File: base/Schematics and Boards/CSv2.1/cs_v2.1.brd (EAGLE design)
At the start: 38.1 x 47 mm, 77 parts, among them J101 J-JTAG-CORTEX-NEEDLE6-LEGS, J301 HIROSE-DF40_50-PIN_CONNECTORS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, J302 HIROSE-DF40_50-PIN_CONNECTORS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, Q1 DMG3415UFY4Q-7F, U1 NCP708MU330TAG, U101 ATSAMD51, U2 W25N01GVZEIG, U201 COULOMB-MAX17262, U202 MAX77827BEWC+T, U203 SENSOR-SI7006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

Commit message: CS-main-v2.1 Routed to completion
Still need to add ground plugs.
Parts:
- moved C111 0.41 mm to (22.8, 19.5)
- moved C105 0.41 mm to (21.8, 19.5)
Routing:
- net GND: track 17.2 -> 207.0 mm, vias 4 -> 13
- net NRESET: track 0.00 -> 54.4 mm, vias 0 -> 2
- net DBG_SWCLK: track 0.00 -> 41.9 mm, vias 0 -> 3
- net DBG_SWDIO: track 0.00 -> 40.5 mm, vias 0 -> 4
- net DBG_TRACE_D0/GPIO13: track 0.00 -> 37.1 mm, vias 0 -> 1
- net DBG_DTR1_V_SENSE: track 0.00 -> 33.8 mm, vias 0 -> 2
- net DBG_DTR0_V_SENSE: track 0.00 -> 31.4 mm, vias 0 -> 2
- net DTR_MSTR_I2C_SCL_SERCOM7_P1: track 81.5 -> 110.9 mm, vias 2 -> 6
- net DBG_PROC_V_SENSE: track 1.91 -> 30.4 mm, vias 0 -> 1
- net DBG_GPIO4/SERCOM6_P0: track 0.00 -> 27.5 mm, vias 0 -> 2
- net DBG_GPIO6/SERCOM6_P2: track 0.00 -> 25.9 mm, vias 0 -> 2
- net DBG_TRACE_D2/GPIO15: track 0.00 -> 25.9 mm, vias 0 -> 3
- net STOR_QSPI_D3: track 0.00 -> 25.8 mm, vias 0 -> 2
- net DBG_SERIAL_RX_SERCOM4: track 0.00 -> 25.0 mm, vias 0 -> 3
- net DTR_MSTR_I2C_SDA_SERCOM7_P0: track 80.0 -> 104.8 mm, vias 2 -> 5
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
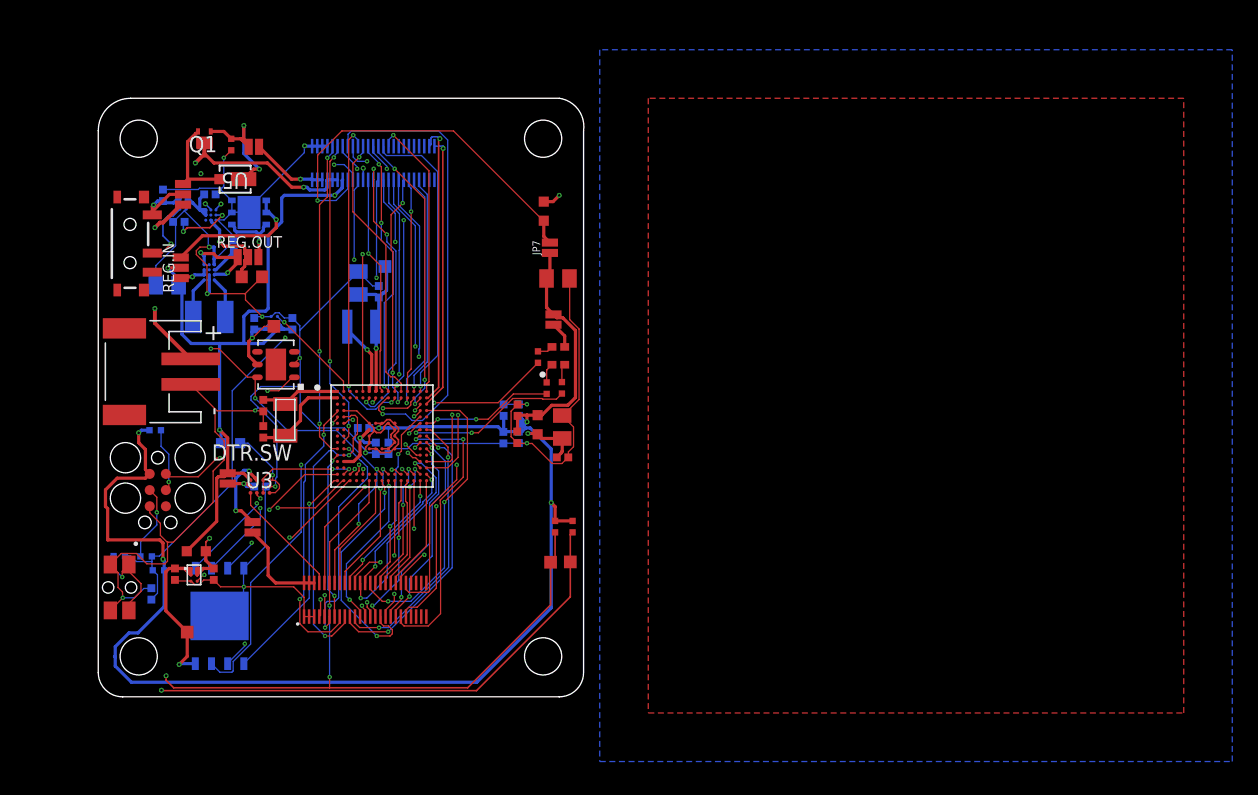
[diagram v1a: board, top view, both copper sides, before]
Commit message: CS_main-v2.1: Finish routing, add ground plugs, and fix DRC errors
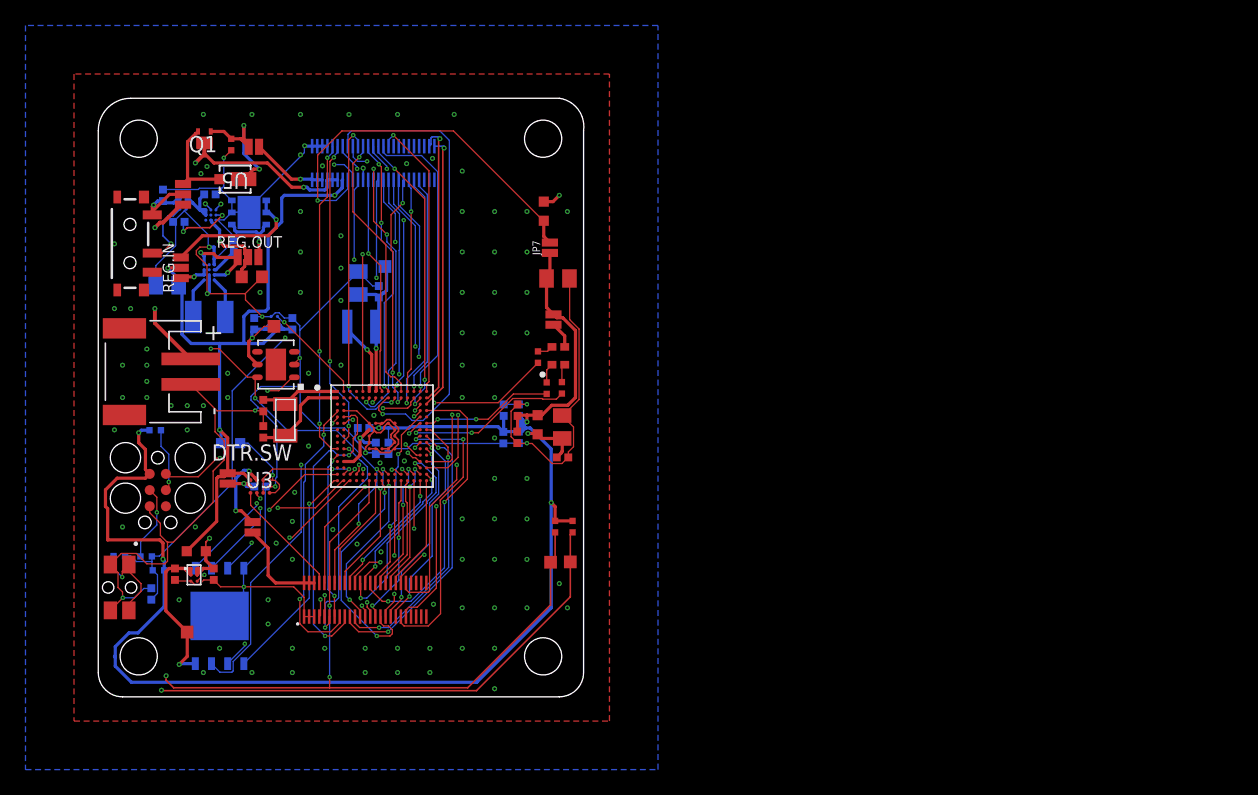
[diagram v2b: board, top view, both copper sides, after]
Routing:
- net GND: vias 13 -> 113
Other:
- board text added: "Screw holes at 115 mil for M2.5 screws of ~94 mil diameter. Estimate 200mil diameter for standoffs/spacers, within which vias should be avoided to prevent unexpected connections between boards if metal spacers are used."
- board text removed: "Screw holes at 90 mil for M2 screws of ~79 mil diameter. M2 screw heads are approx 150 mil diameter. There must be appropriate space for this Standoff diameter should be <= 175mil. Wurth Electronik makes viable standoffs"

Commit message: Gerbers, BOM, and minor part changes
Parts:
- L201: device Inductors:L1008 -> Inductors:XAL40
- moved C205 0.84 mm to (4.57, 32.4)
- moved L201 0.34 mm to (8.56, 29.5)
- renumbered JP7 to JP.PROC
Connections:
- net BB_LX1: now also L201.2; no longer L201.1
- net BB_LX2: now also L201.1; no longer L201.2
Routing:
- net +3V3: track 77.4 -> 79.2 mm
- net GND: track 207.0 -> 207.8 mm, vias 113 -> 116

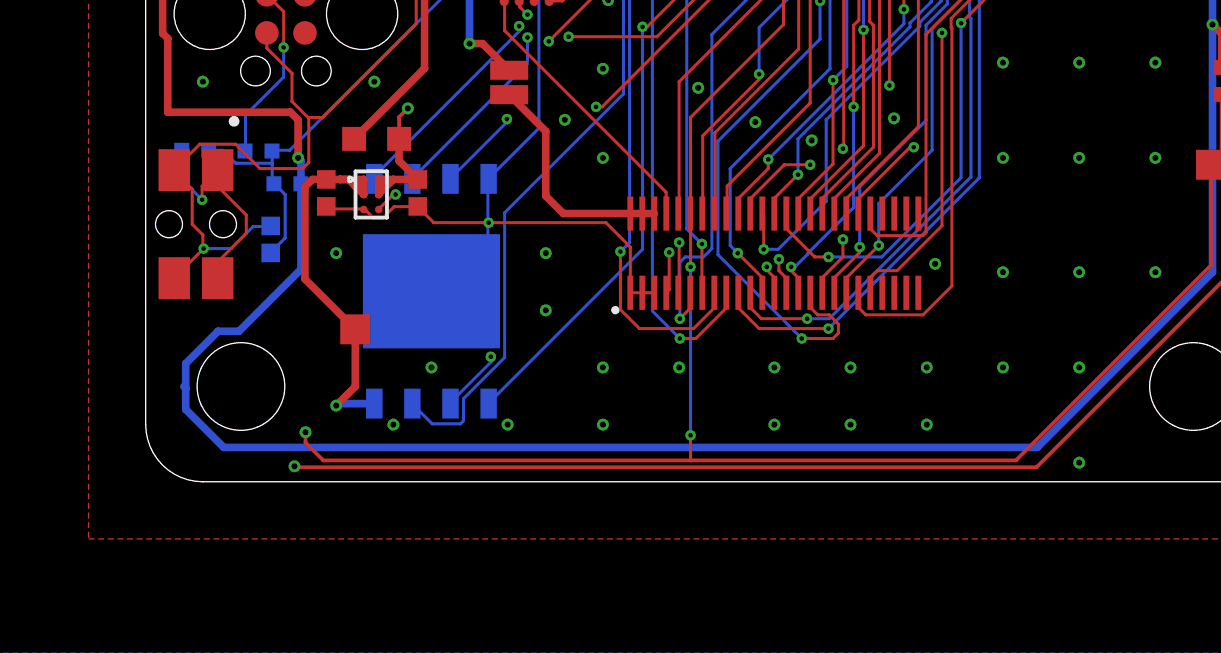
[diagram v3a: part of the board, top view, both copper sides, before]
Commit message: BASE: move vias from screw holes and regen gerbers
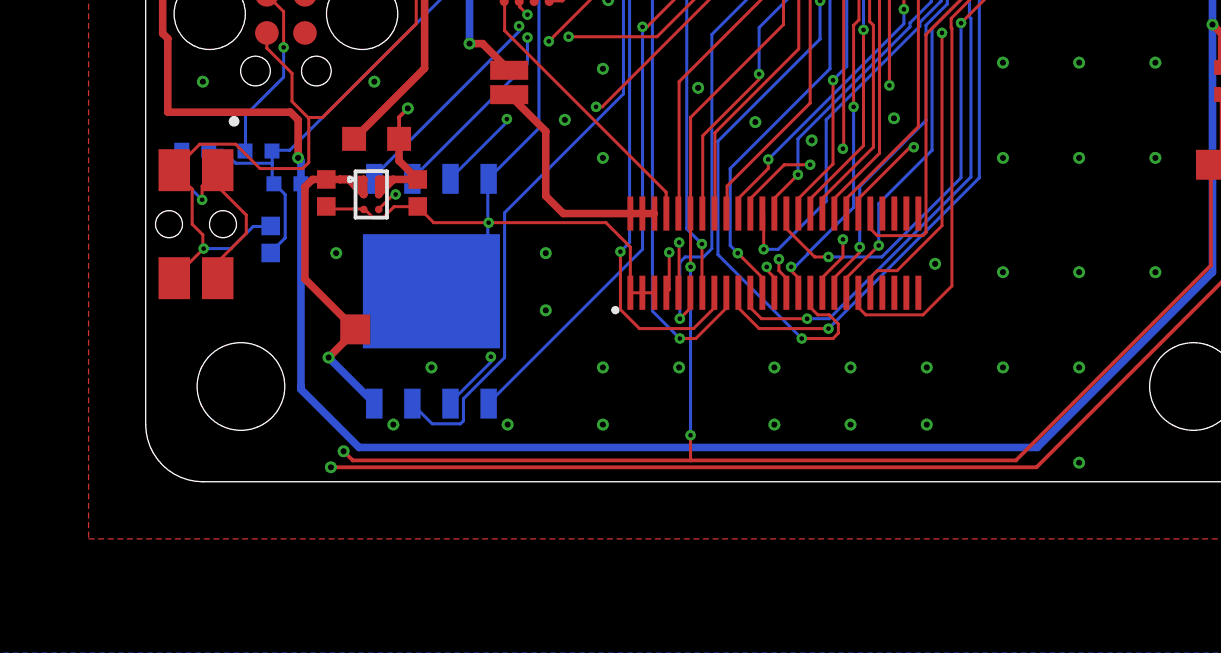
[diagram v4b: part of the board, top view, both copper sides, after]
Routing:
- net +3V3_PROC: track 130.7 -> 124.4 mm
- net DTR_MSTR_I2C_SCL_SERCOM7_P1: track 111.4 -> 110.7 mm
- net +3V3_STOR: track 13.5 -> 12.9 mm
- net DTR_MSTR_I2C_SDA_SERCOM7_P0: track 104.8 -> 104.2 mm

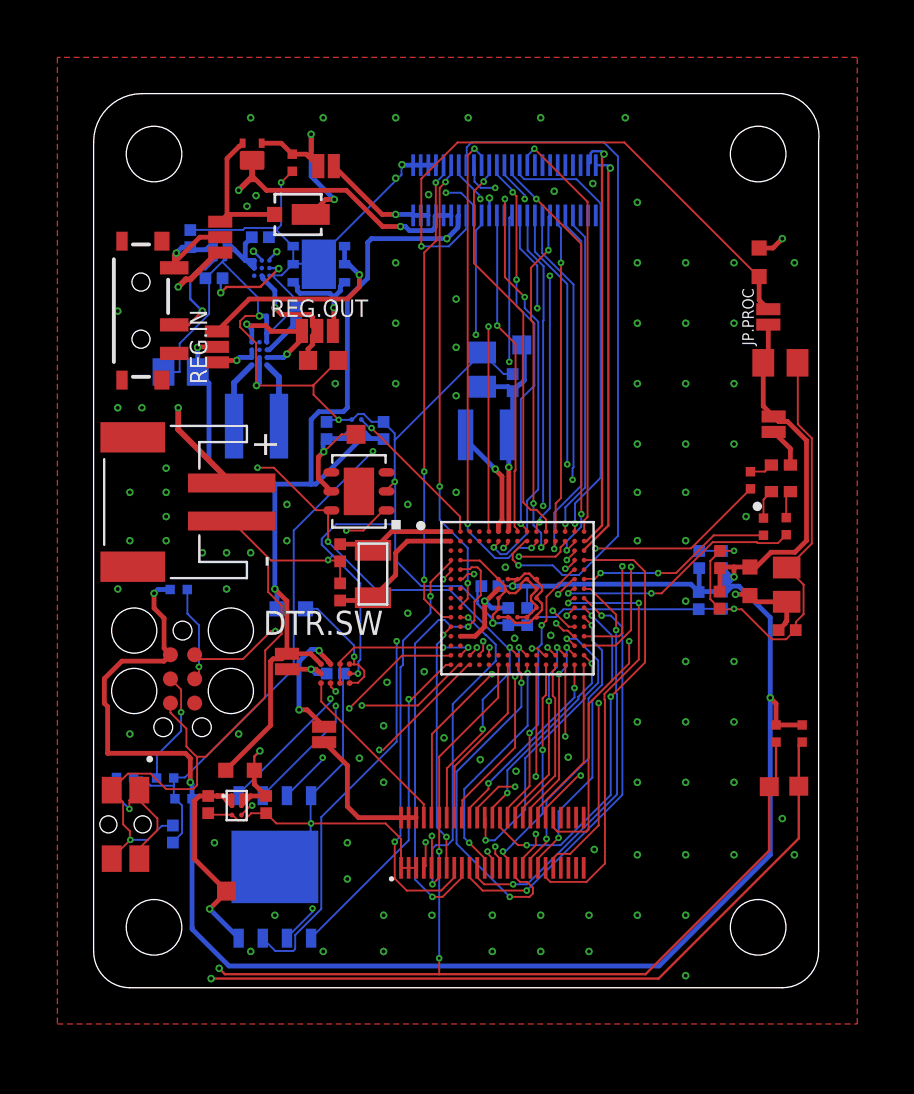
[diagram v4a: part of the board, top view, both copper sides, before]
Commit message: BASE: Increase holes sizes for snap-lock inter-board connectors
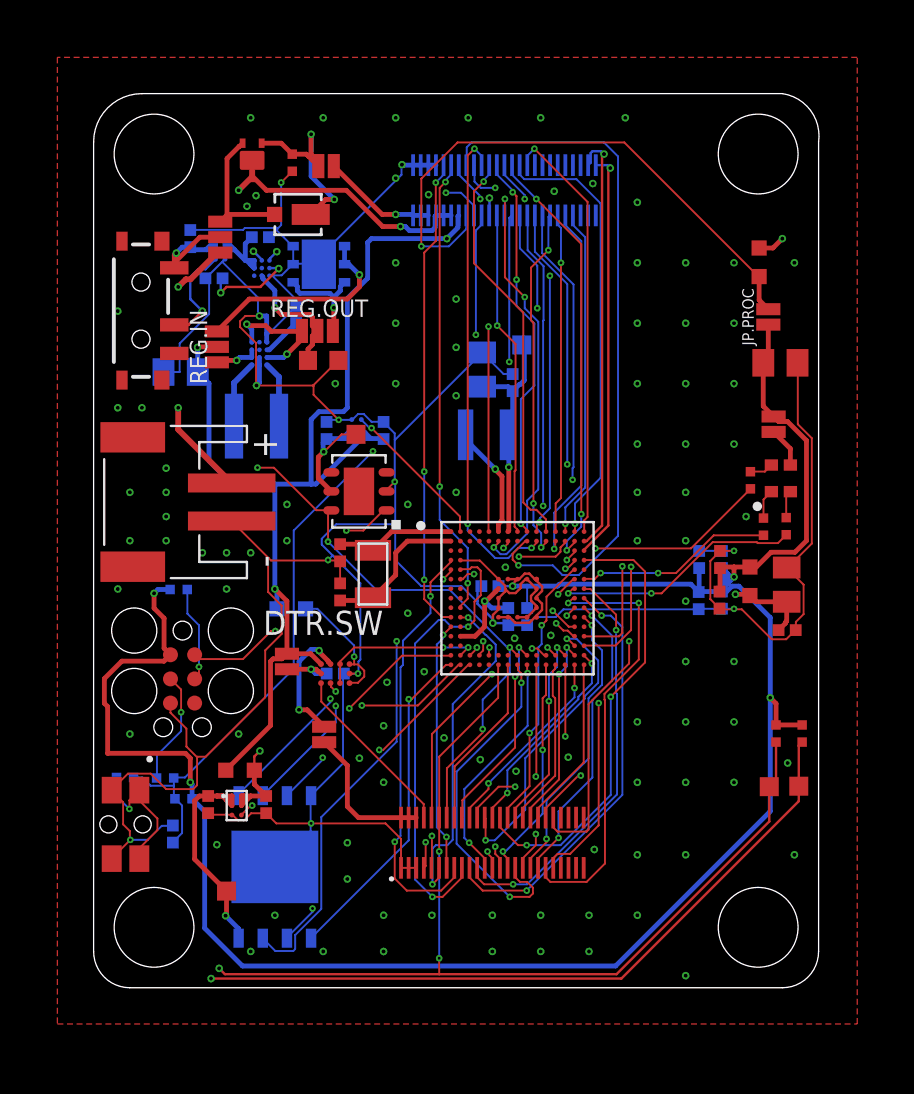
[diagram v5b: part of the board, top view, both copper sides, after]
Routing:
- net DTR_MSTR_I2C_SCL_SERCOM7_P1: track 110.7 -> 108.9 mm
- net +3V3_PROC: track 124.4 -> 122.7 mm
- net DTR_MSTR_I2C_SDA_SERCOM7_P0: track 104.2 -> 102.7 mm
- net +3V3_STOR: track 12.9 -> 12.2 mm
- net GND: vias 116 -> 114
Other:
- board text added: "Holes to 165 for plastic snap locks"

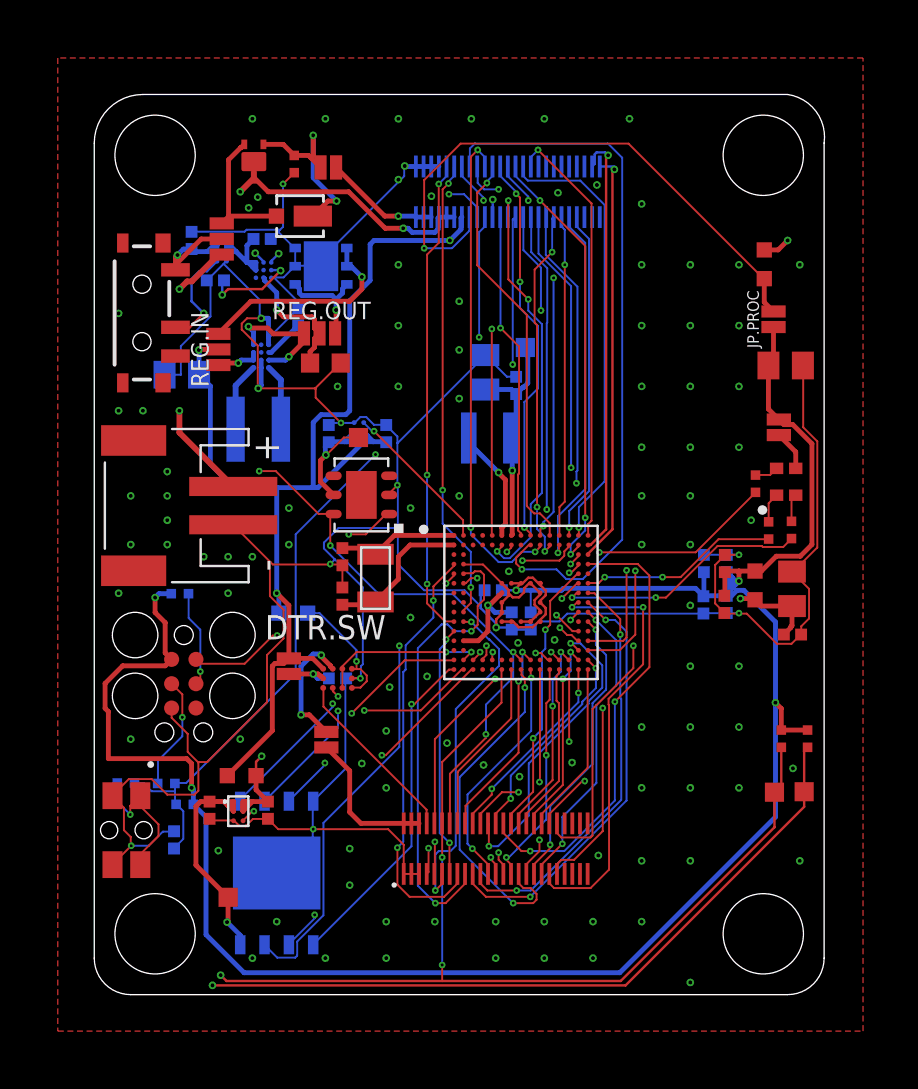
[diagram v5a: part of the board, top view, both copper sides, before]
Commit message: Update files per design review and regenerate CAM
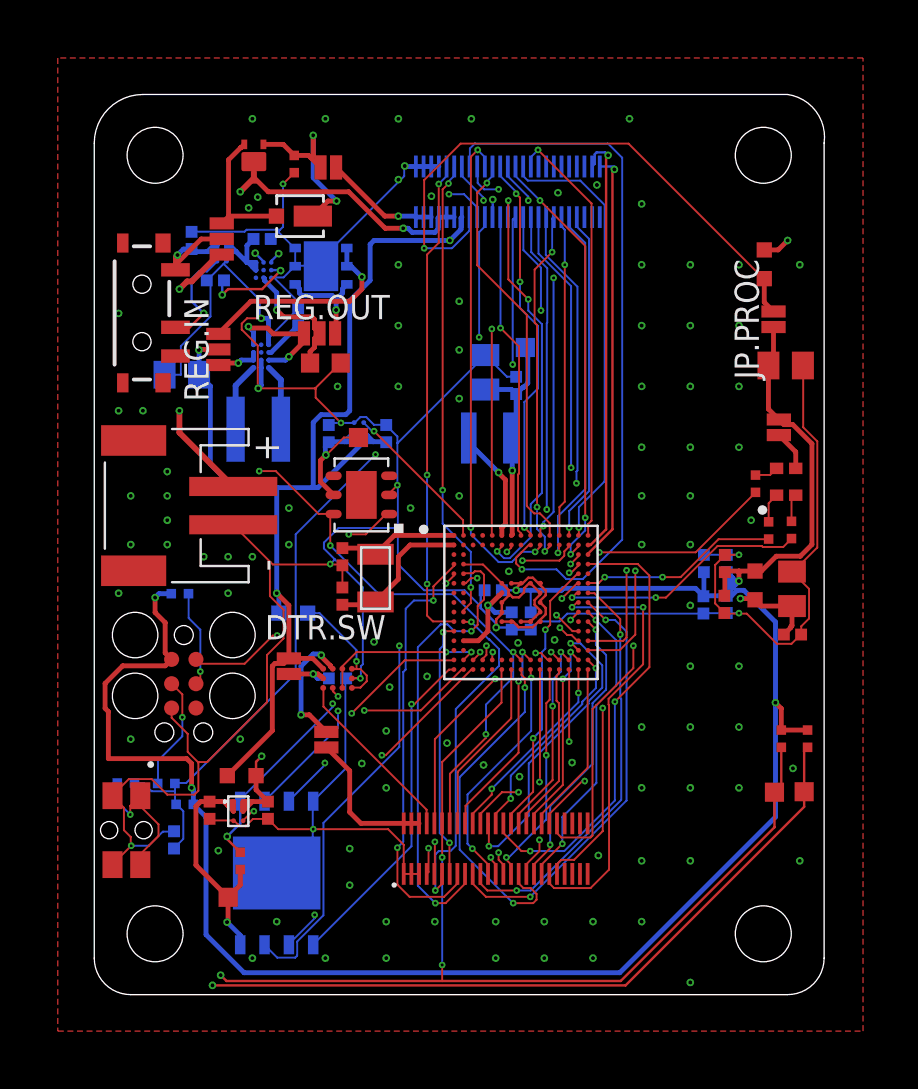
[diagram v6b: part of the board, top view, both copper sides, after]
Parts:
- added R3: 100k, Resistors:R0402
- R207: value 0.51 -> 0.24
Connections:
- net +3V3_STOR: now also R3.1
- net STOR_QSPI_CS: now also R3.2
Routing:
- net STOR_QSPI_CS: track 17.0 -> 20.2 mm, vias 2 -> 3
- net +3V3_STOR: track 12.2 -> 13.9 mm
- net DTR_BUS2_AIN0/GPIO2: track 22.1 -> 22.7 mm
- net GND: vias 114 -> 113

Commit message: STACK: Generate Gerbers, format BOM, manage directories
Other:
- board text removed: "Holes to 165 for plastic snap locks"
